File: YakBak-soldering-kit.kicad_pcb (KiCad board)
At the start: 2 copper layers, 33.1 x 68 mm, 13 parts, among them J1 Conn_01x07_Socket, J2 Conn_01x07_Socket, SW1 Say, SW2 Play, U1 MOUDLE-SEEEDUINO-XIAO-ESP32C3, U2 Electret Microphone Amp Module, U3 Adafruit 2130 - PAM8302

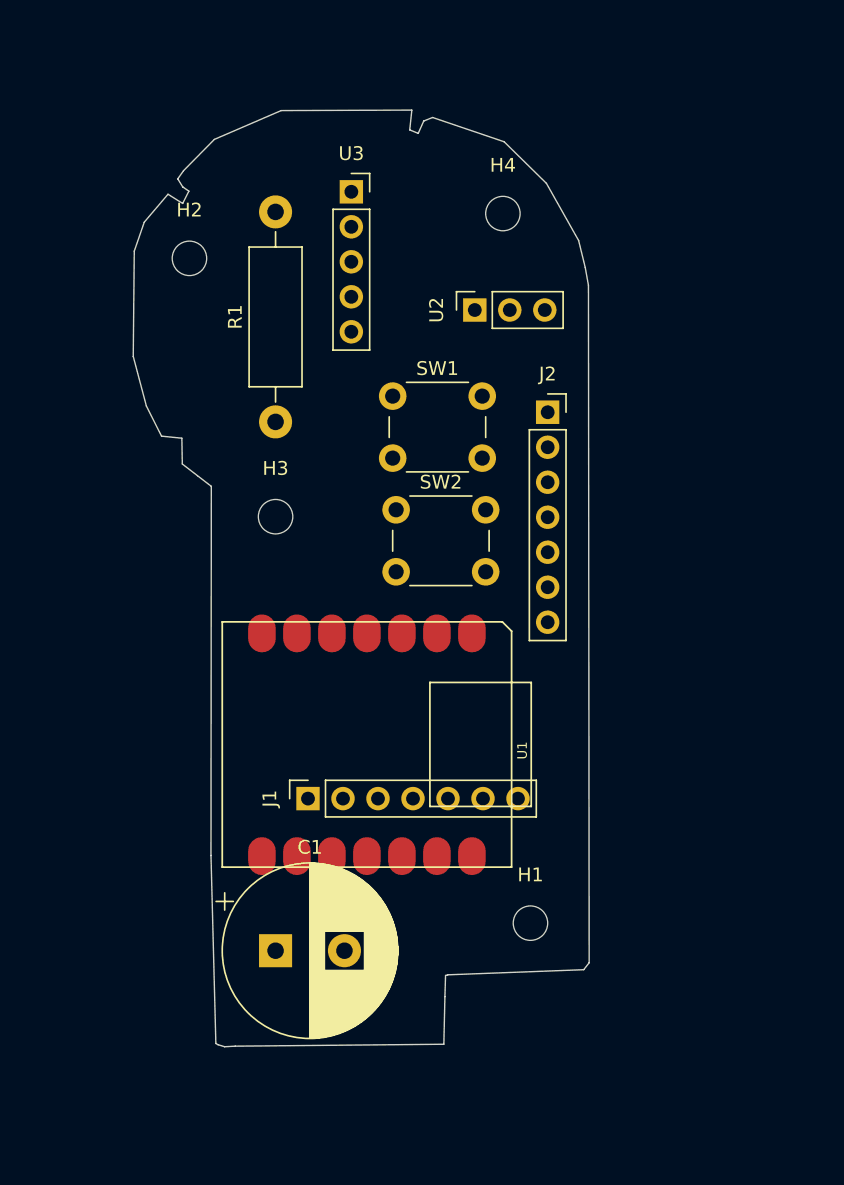
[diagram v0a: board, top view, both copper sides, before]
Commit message: finished draft layout and updated missing symbols/footprints
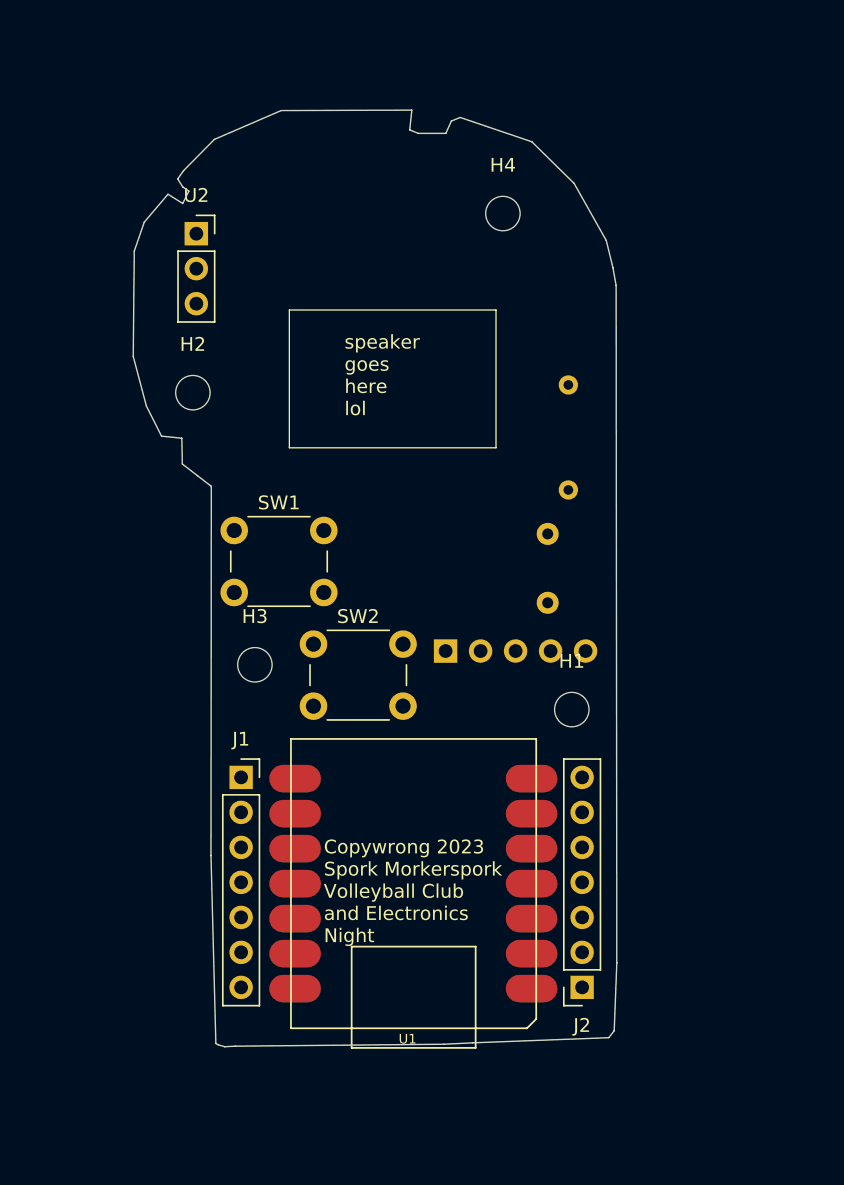
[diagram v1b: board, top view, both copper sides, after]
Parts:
- C1: footprint Capacitor_THT:CP_Radial_D12.5mm_P5.00mm -> Capacitor_THT:C_Disc_D5.1mm_W3.2mm_P5.00mm; moved to B.Cu
- R1: footprint Resistor_THT:R_Axial_DIN0411_L9.9mm_D3.6mm_P15.24mm_Horizontal -> Resistor_THT:R_Axial_DIN0204_L3.6mm_D1.6mm_P7.62mm_Horizontal; moved to B.Cu
- U1: footprint XIAO_ESP32C3_PCB:MOUDLE14P-SMD-2.54-21X17.8MM -> xiao ESP32C3_PCB:MOUDLE14P-SMD-2.54-21X17.8MM
- U3: footprint Connector_PinSocket_2.54mm:PinSocket_1x05_P2.54mm_Vertical -> Connector_PinHeader_2.54mm:PinHeader_1x05_P2.54mm_Vertical; moved to B.Cu
- moved J2 41.8 mm to (122.2, 109.7), turned to 180 degrees
- moved U3 34.0 mm to (112.3, 85.2), turned to -90 degrees
- moved C1 32.1 mm to (119.8, 81.8), turned to 90 degrees
- moved U1 24.3 mm to (118.9, 91.6), turned to 180 degrees
- moved R1 21.8 mm to (121.2, 73.6)
- moved U2 21.0 mm to (94.2, 55.0), turned to 0 degrees
- moved H1 15.8 mm to (121.5, 89.5)
- moved SW1 15.1 mm to (97.0, 76.5)
- moved SW2 11.4 mm to (102.8, 84.8)
- moved H3 10.9 mm to (98.5, 86.2)
- moved H2 9.75 mm to (94.0, 66.5)
- moved J1 5.09 mm to (97.5, 94.4), turned to 0 degrees
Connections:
- U2 pad 1: (no net) -> /D0
- U2 pad 2: (no net) -> GND
- U2 pad 3: (no net) -> +3.3V
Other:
- board size 33.1 x 68 mm -> 35.1 x 68 mm
- board text added: "Copywrong 2023 Spork Morkerspork Volleyball Club and Electronics Night"
- board text added: "speaker goes here lol"

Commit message: added artwork and routed traces
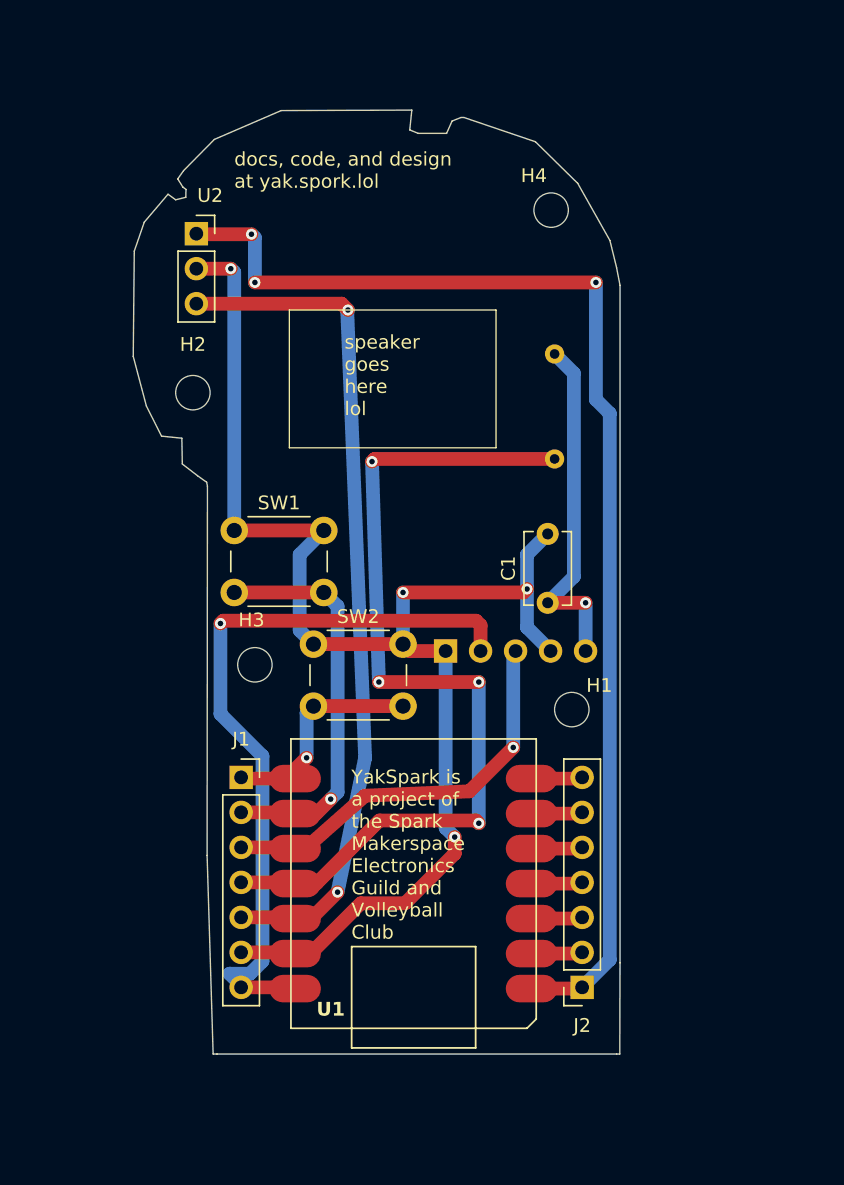
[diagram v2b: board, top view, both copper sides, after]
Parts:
- C1: moved to F.Cu
- moved H4 3.51 mm to (120.0, 53.2)
- moved R1 2.46 mm to (120.2, 71.3)
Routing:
- net GND: track 0.00 -> 103.5 mm, vias 0 -> 4
- net /D0: track 0.00 -> 88.5 mm, vias 0 -> 3
- net /D10: track 0.00 -> 66.1 mm, vias 0 -> 4
- net +3.3V: track 0.00 -> 61.5 mm, vias 0 -> 2
- net +5V: track 0.00 -> 54.8 mm, vias 0 -> 1
- net /D9: track 0.00 -> 29.6 mm, vias 0 -> 1
- net /D8: track 0.00 -> 29.1 mm, vias 0 -> 1
- net Net-(U3-A+): track 0.00 -> 25.7 mm, vias 0 -> 1
- net /D7: track 0.00 -> 16.3 mm, vias 0 -> 1
- net /D5: track 0.00 -> 3.71 mm
- net /D6: track 0.00 -> 3.71 mm
- net /D4: track 0.00 -> 3.71 mm
- net /D3: track 0.00 -> 3.71 mm
- net /D2: track 0.00 -> 3.71 mm
- net /D1: track 0.00 -> 3.71 mm
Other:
- board size 35.1 x 68 mm -> 35.3 x 68.5 mm
- board text added: "YakSpark is a project of the Spark Makerspace Electronics Guild and Volleyball Club"
- board text added: "docs, code, and design at yak.spork.lol"
- board text removed: "Copywrong 2023 Spork Morkerspork Volleyball Club and Electronics Night"

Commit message: add ground fill to F.Cu
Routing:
- added copper zone on F.Cu, net GND
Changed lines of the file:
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@@
   (segment (start 105.2 60.55) (end 105.25 60.5) (width 1) (layer "B.Cu") (net 15))
   (segment (start 104.5 102.75) (end 106.5 93) (width 1) (layer "B.Cu") (net 15))
+  (zone (net 2) (net_name "GND") (layer "F.Cu") (hatch edge 0.5)
+    (connect_pads (clearance 0.5))
+    (min_thickness 0.25) (filled_areas_thickness no)
+    (fill yes (thermal_gap 0.5) (thermal_bridge_width 0.5))
+    (polygon
+      (pts
+        (xy 83.25 40)
+        (xy 82 121)
+        (xy 138.25 122)
+        (xy 139.25 43)
+      )
+    )
+  )
   (group "" (id c320bd41-db23-4f12-b313-22fa4e8ab171)
     (members

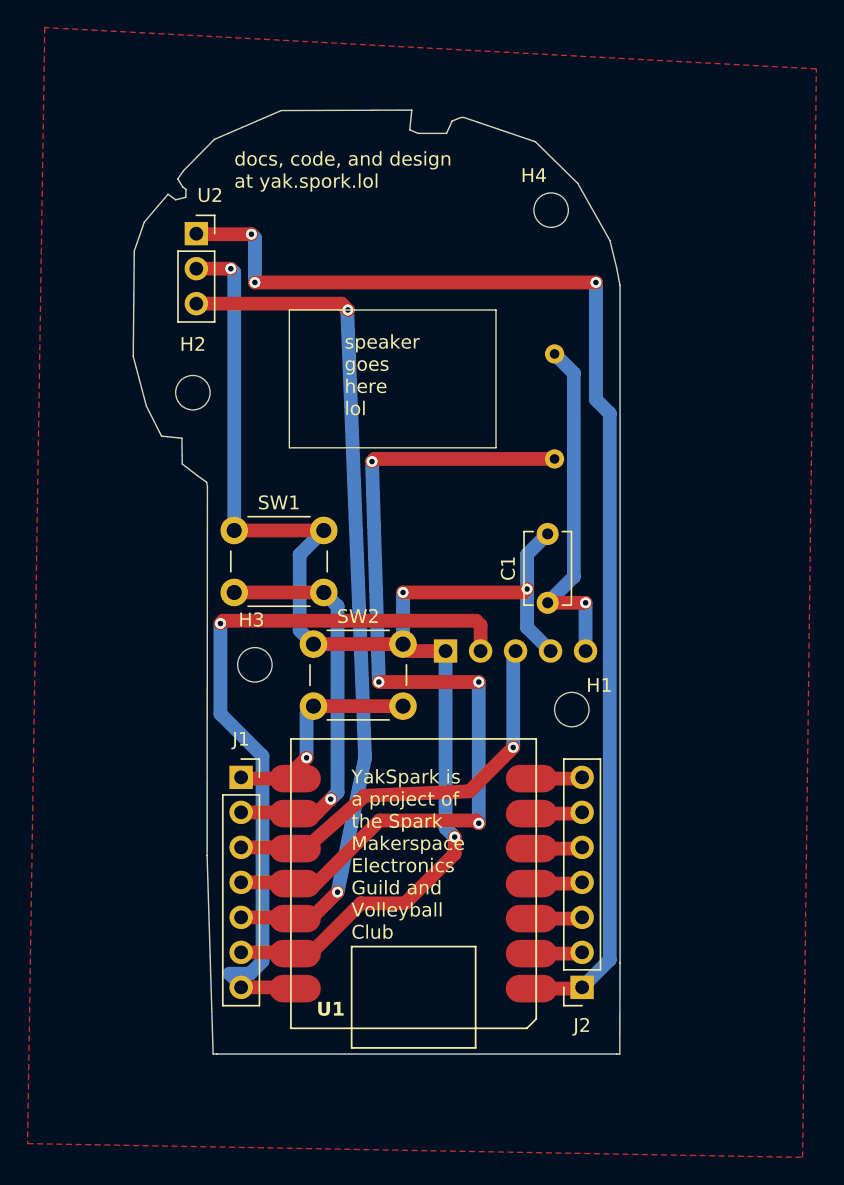
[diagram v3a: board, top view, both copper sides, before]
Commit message: cleaned up, rounded traces, added directions
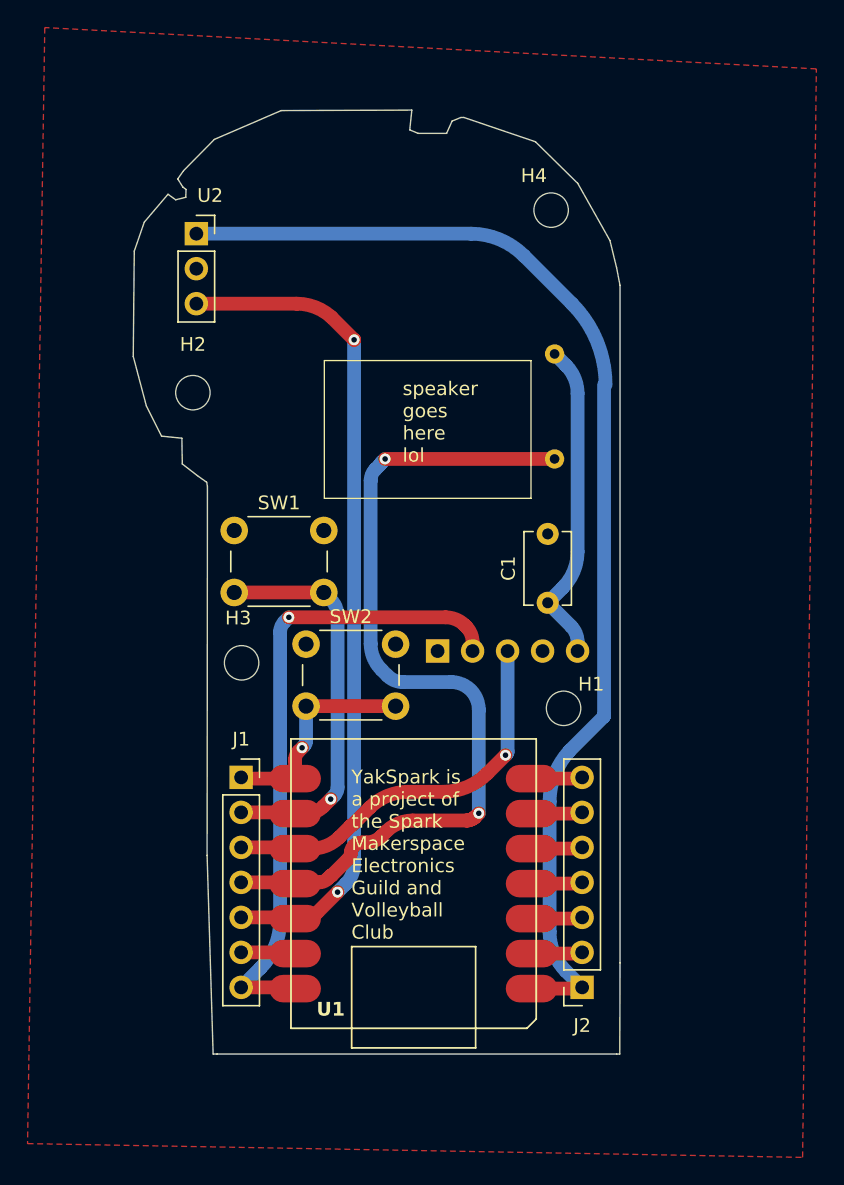
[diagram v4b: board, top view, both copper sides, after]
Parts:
- moved H3 0.97 mm to (97.5, 86.1)
- moved H1 0.60 mm to (120.9, 89.4)
- moved U3 0.58 mm to (111.8, 85.2)
- moved SW2 0.54 mm to (102.2, 84.8)
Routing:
- net GND: track 103.5 -> 4.30 mm, vias 4 -> 0
- net +5V: track 54.8 -> 46.9 mm
- net /D0: track 88.5 -> 85.2 mm, vias 3 -> 0
- net /D10: track 66.1 -> 63.4 mm, vias 4 -> 2
- net Net-(U3-A+): track 25.7 -> 23.7 mm, vias 1 -> 0
- net +3.3V: track 61.5 -> 60.6 mm
- net /D9: track 29.6 -> 29.1 mm
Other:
- board text added: "1. Solder ESP module 2. Solder buttons, capacitor, and resistor 3. Solder amplifier module 4. Connect and stick speaker 5. Solder mic module 6. Program it!"
- board text added: "R1"
